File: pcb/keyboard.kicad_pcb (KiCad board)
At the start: 2 copper layers, 21 parts, among them SW1 SW_Push, SW10 RotaryEncoder_Switch, SW2 SW_Push, SW3 SW_Push, SW4 SW_Push, SW5 SW_Push, SW6 SW_Push, SW7 SW_Push, SW8 SW_Push, SW9 SW_Push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

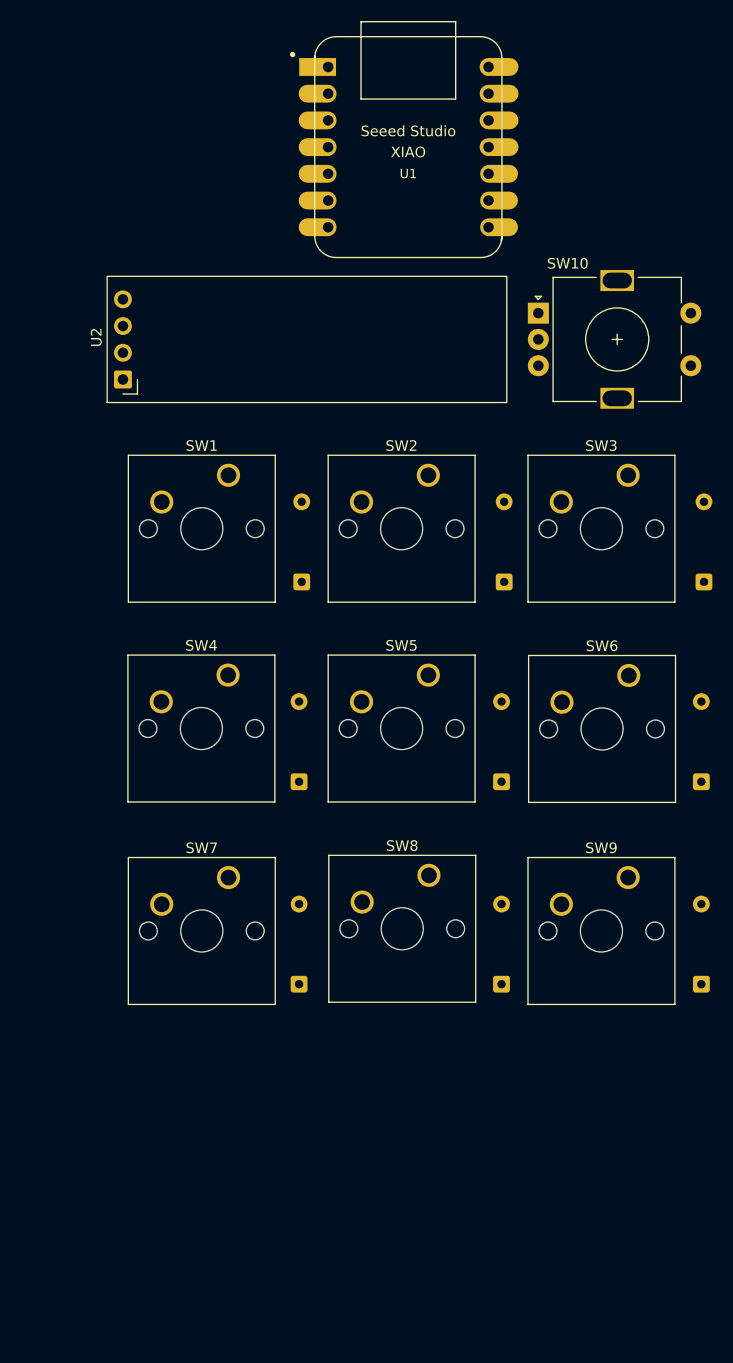
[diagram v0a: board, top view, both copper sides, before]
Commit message: connect switches to the microcontroller
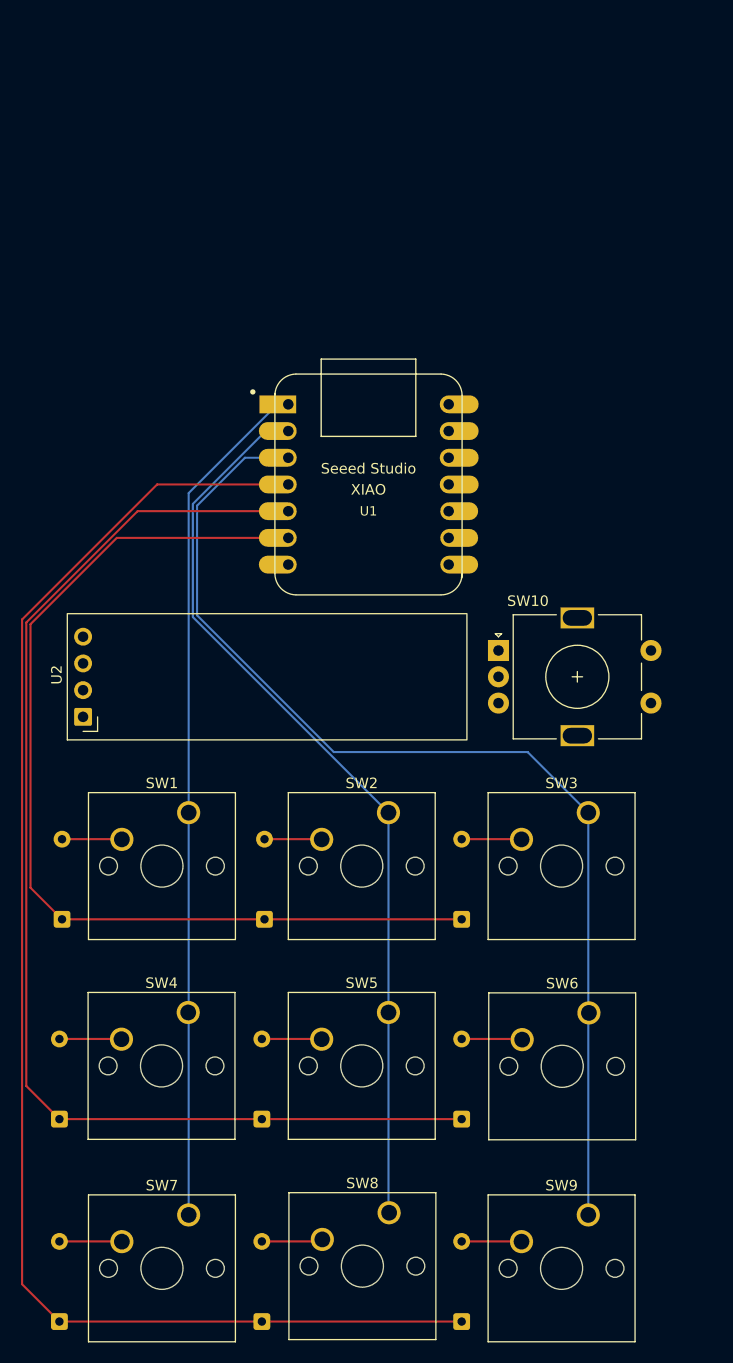
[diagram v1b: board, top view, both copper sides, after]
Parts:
- moved D3 39.5 mm to (131.2, 96.1)
- moved D1 39.4 mm to (93.2, 96.1)
- moved D2 39.4 mm to (112.5, 96.1)
- moved D4 39.4 mm to (93.0, 115.1)
- moved D5 39.4 mm to (112.2, 115.1)
- moved D6 39.4 mm to (131.2, 115.1)
- moved D7 39.4 mm to (93.0, 134.4)
- moved D8 39.4 mm to (112.2, 134.4)
- moved D9 39.4 mm to (131.2, 134.4)
- moved SW6 32.3 mm to (143.3, 105.0)
- moved SW8 32.3 mm to (124.3, 124.0)
- moved SW1 32.3 mm to (105.2, 86.0)
- moved SW10 32.3 mm to (134.7, 70.6)
- moved SW2 32.3 mm to (124.2, 86.0)
- moved SW3 32.3 mm to (143.2, 86.0)
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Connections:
- U1 pad 4: Row 0 -> Row 2
- U1 pad 6: Row 2 -> Row 0
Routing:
- net Row 2: track 0.00 -> 137.1 mm
- net Row 1: track 0.00 -> 116.1 mm
- net Column 2: track 0.00 -> 104.2 mm
- net Row 0: track 0.00 -> 95.2 mm
- net Column 1: track 0.00 -> 87.1 mm
- net Column 0: track 0.00 -> 81.6 mm
- net Net-(D7-A): track 0.00 -> 5.95 mm
- net Net-(D4-A): track 0.00 -> 5.91 mm
- net Net-(D8-A): track 0.00 -> 5.83 mm
- net Net-(D6-A): track 0.00 -> 5.77 mm
- net Net-(D5-A): track 0.00 -> 5.70 mm
- net Net-(D1-A): track 0.00 -> 5.70 mm
- net Net-(D9-A): track 0.00 -> 5.70 mm
- net Net-(D3-A): track 0.00 -> 5.70 mm
- net Net-(D2-A): track 0.00 -> 5.45 mm

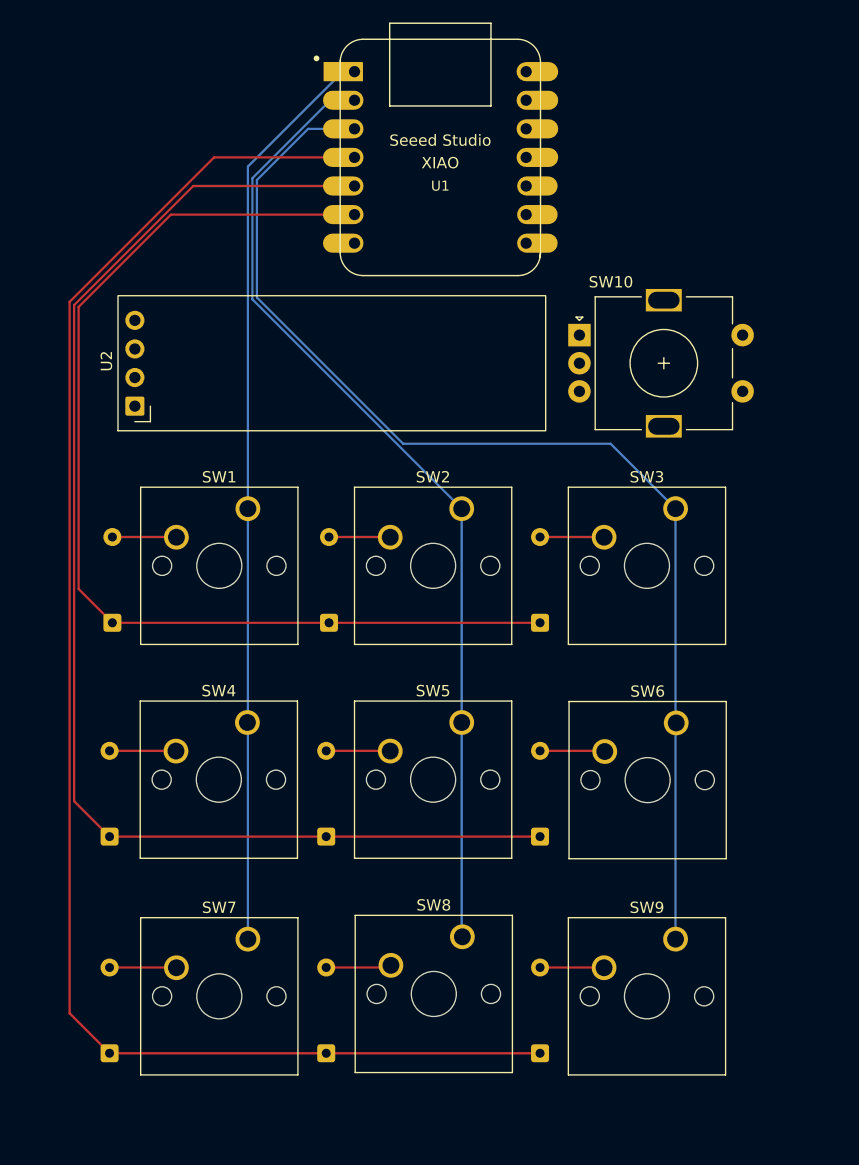
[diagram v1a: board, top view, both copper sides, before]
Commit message: connect all components on schematic; remove invalid connections on pcb
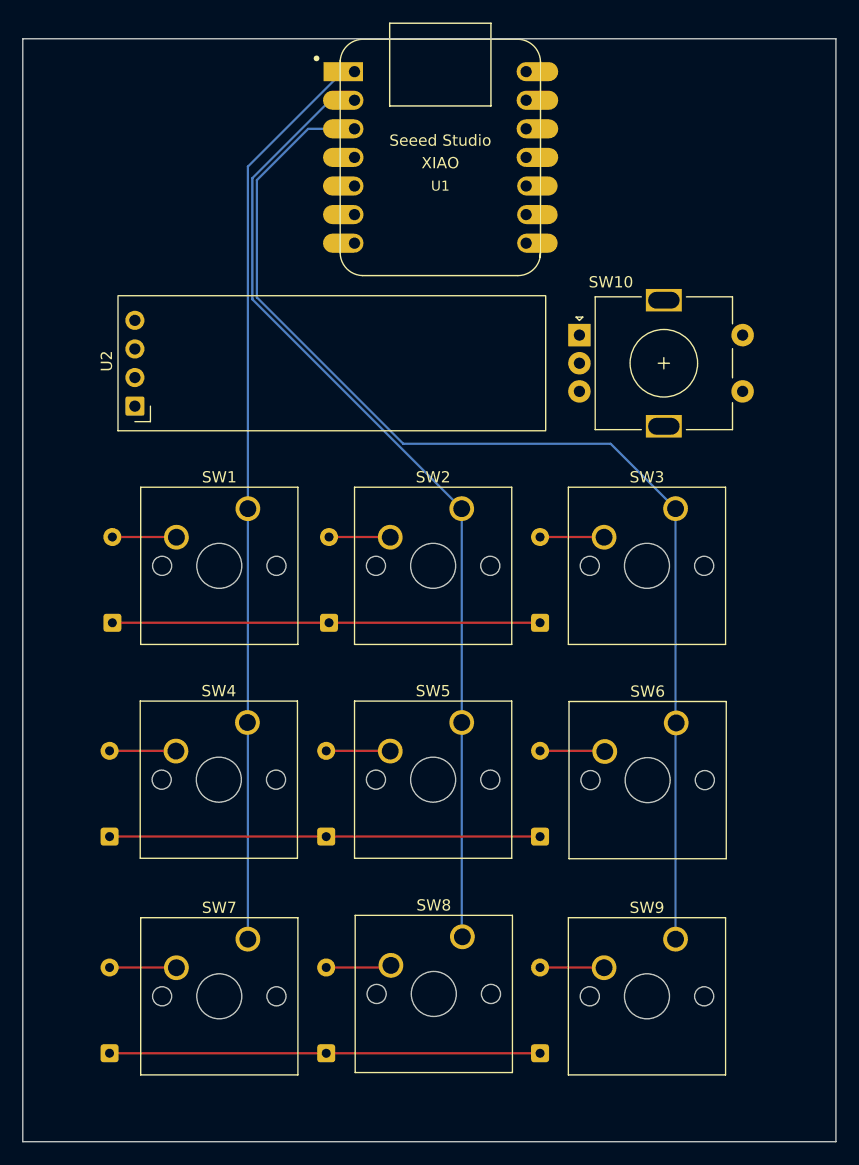
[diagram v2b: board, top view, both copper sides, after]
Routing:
- net Row 2: track 137.1 -> 38.3 mm
- net Row 1: track 116.1 -> 38.3 mm
- net Row 0: track 95.2 -> 38.0 mm
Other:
- board outline added: 72.2 x 98 mm
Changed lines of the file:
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@@
 		)
+	)
+	(gr_rect
+		(start 85.25 44.25)
+		(end 157.5 142.25)
+		(stroke
+			(width 0.05)
+			(type default)
+		)
+		(fill no)
+		(layer "Edge.Cuts")
 	)
 	(segment
@@
 	)
 	(segment
-		(start 90.21 68.08)
-		(end 90.21 93.14)
-		(width 0.2)
-		(layer "F.Cu")
-		(net "Row 0")
-	)
-	(segment
 		(start 93.21 96.14)
 		(end 131.21 96.14)
-		(width 0.2)
-		(layer "F.Cu")
-		(net "Row 0")
-	)
-	(segment
-		(start 98.417985 59.872015)
-		(end 90.21 68.08)
-		(width 0.2)
-		(layer "F.Cu")
-		(net "Row 0")
-	)
-	(segment
-		(start 114.7245 59.872015)
-		(end 98.417985 59.872015)
-		(width 0.2)
-		(layer "F.Cu")
-		(net "Row 0")
-	)
-	(segment
-		(start 90.21 93.14)
-		(end 93.21 96.14)
 		(width 0.2)
 		(layer "F.Cu")
@@
 		(start 92.96 115.14)
 		(end 131.21 115.14)
-		(width 0.2)
-		(layer "F.Cu")
-		(net "Row 1")
-	)
-	(segment
-		(start 114.7245 57.332015)
-		(end 100.3923 57.332015)
-		(width 0.2)
-		(layer "F.Cu")
-		(net "Row 1")
-	)
-	(segment
-		(start 100.3923 57.332015)
-		(end 89.81 67.914315)
-		(width 0.2)
-		(layer "F.Cu")
-		(net "Row 1")
-	)
-	(segment
-		(start 89.81 67.914315)
-		(end 89.81 111.99)
-		(width 0.2)
-		(layer "F.Cu")
-		(net "Row 1")
-	)
-	(segment
-		(start 89.81 111.99)
-		(end 92.96 115.14)
 		(width 0.2)
 		(layer "F.Cu")
@@
 	)
 	(segment
-		(start 89.41 67.63)
-		(end 89.41 130.84)
-		(width 0.2)
-		(layer "F.Cu")
-		(net "Row 2")
-	)
-	(segment
-		(start 102.247985 54.792015)
-		(end 89.41 67.63)
-		(width 0.2)
-		(layer "F.Cu")
-		(net "Row 2")
-	)
-	(segment
-		(start 89.41 130.84)
-		(end 92.96 134.39)
-		(width 0.2)
-		(layer "F.Cu")
-		(net "Row 2")
-	)
-	(segment
-		(start 114.7245 54.792015)
-		(end 102.247985 54.792015)
-		(width 0.2)
-		(layer "F.Cu")
-		(net "Row 2")
-	)
-	(segment

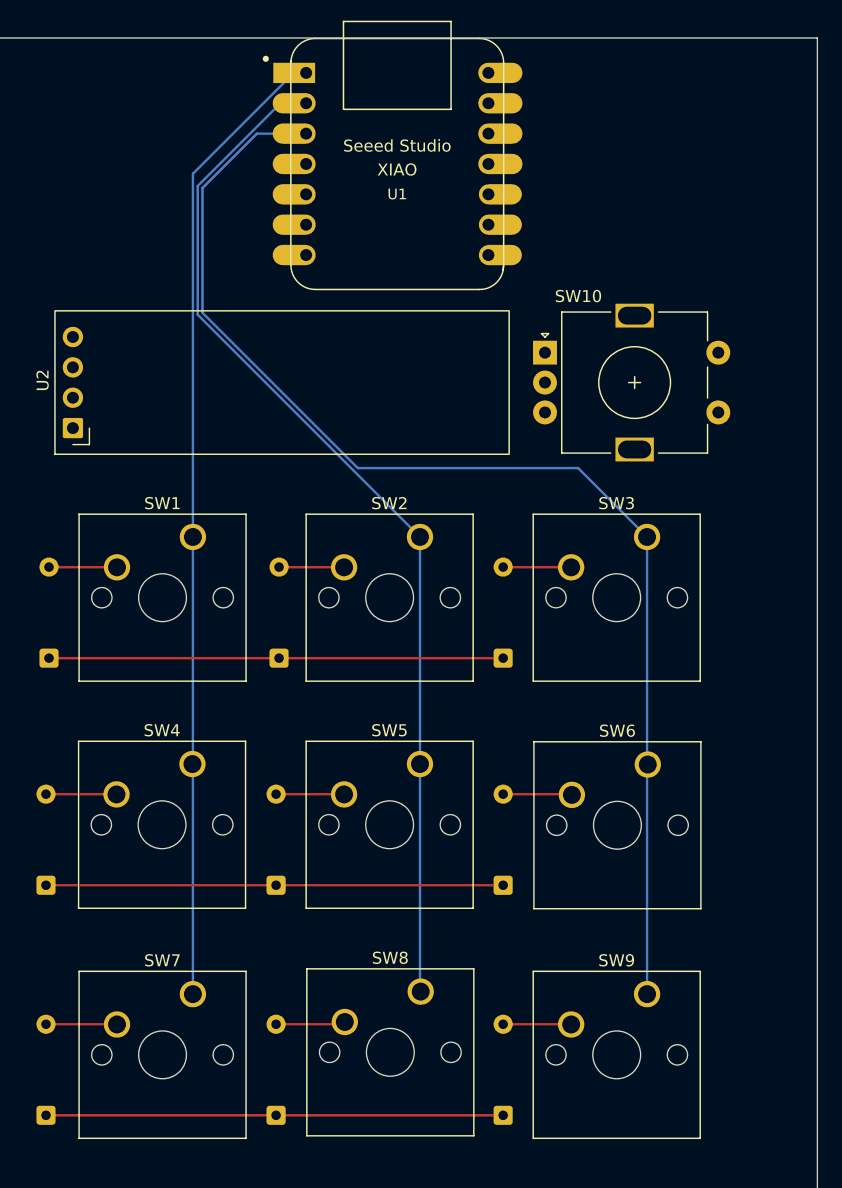
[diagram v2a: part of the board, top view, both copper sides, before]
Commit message: connect everything on the pcb
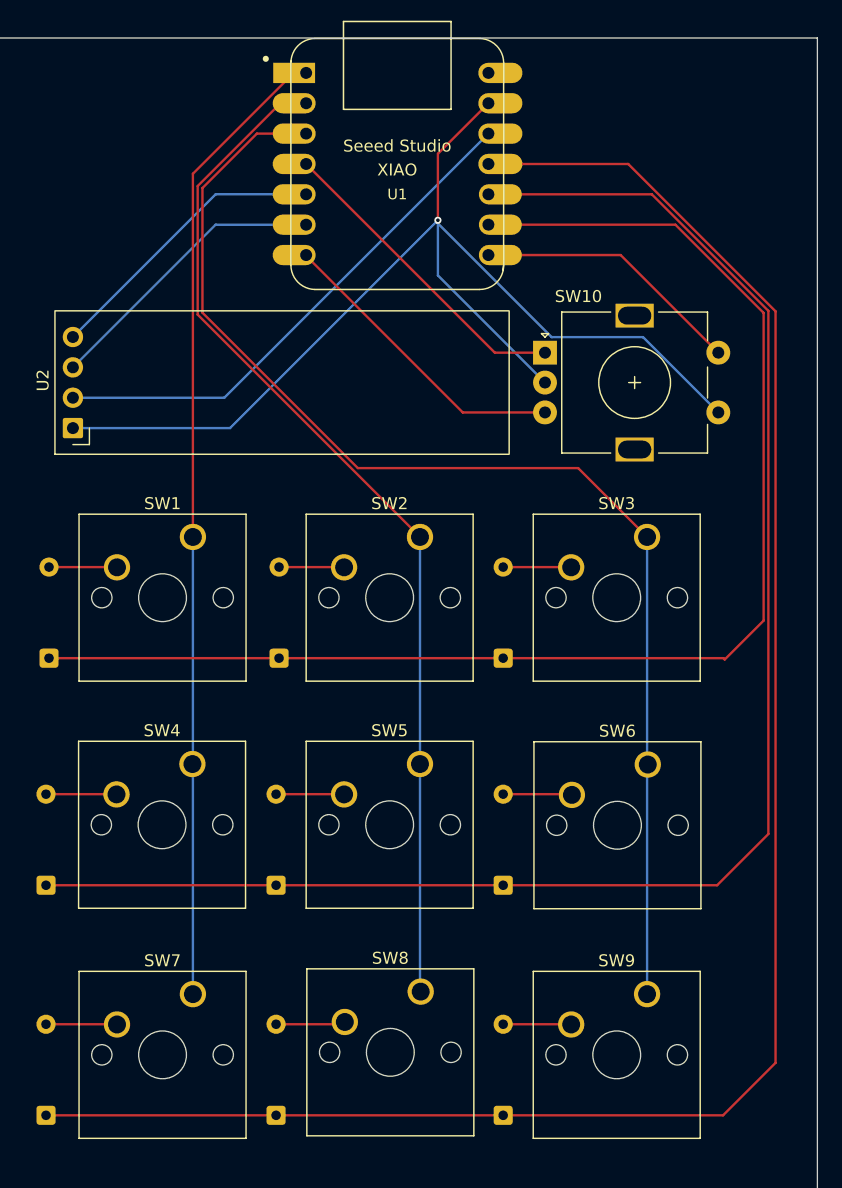
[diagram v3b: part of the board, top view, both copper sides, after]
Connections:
- SW10 pad A: unconnected-(SW10-PadA) -> ROT A
- SW10 pad B: unconnected-(SW10-PadB) -> ROT B
- SW10 pad C: unconnected-(SW10-PadC) -> GND
- SW10 pad S1: unconnected-(SW10-PadS1) -> GND
- SW10 pad S2: unconnected-(SW10-PadS2) -> ROT SWITCH
- U1 pad 10: unconnected-(U1-PA5_A9_D9_MISO-Pad10) -> Row 1
- U1 pad 11: unconnected-(U1-PA6_A10_D10_MOSI-Pad11) -> Row 2
- U1 pad 12: unconnected-(U1-3V3-Pad12) -> VCC
- U1 pad 13: unconnected-(U1-GND-Pad13) -> GND
- U1 pad 4: Row 2 -> ROT A
- U1 pad 5: Row 1 -> SDA
- U1 pad 6: Row 0 -> SCL
- U1 pad 7: unconnected-(U1-PB08_A6_D6_TX-Pad7) -> ROT B
- U1 pad 8: unconnected-(U1-PB09_A7_D7_RX-Pad8) -> ROT SWITCH
- U1 pad 9: unconnected-(U1-PA7_A8_D8_SCK-Pad9) -> Row 0
- U2 pad 1: unconnected-(U2-GND-Pad1) -> GND
- U2 pad 2: unconnected-(U2-VCC-Pad2) -> VCC
- U2 pad 3: unconnected-(U2-SCL-Pad3) -> SCL
- U2 pad 4: unconnected-(U2-SDA-Pad4) -> SDA
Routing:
- net Row 2: track 38.3 -> 154.9 mm
- net GND: track 0.00 -> 96.8 mm, vias 0 -> 1
- net Row 1: track 38.3 -> 133.4 mm
- net Row 0: track 38.0 -> 113.0 mm
- net VCC: track 0.00 -> 43.9 mm
- net ROT A: track 0.00 -> 26.5 mm
- net ROT B: track 0.00 -> 25.5 mm
- net SCL: track 0.00 -> 24.5 mm
- net SDA: track 0.00 -> 24.5 mm
- net ROT SWITCH: track 0.00 -> 22.6 mm

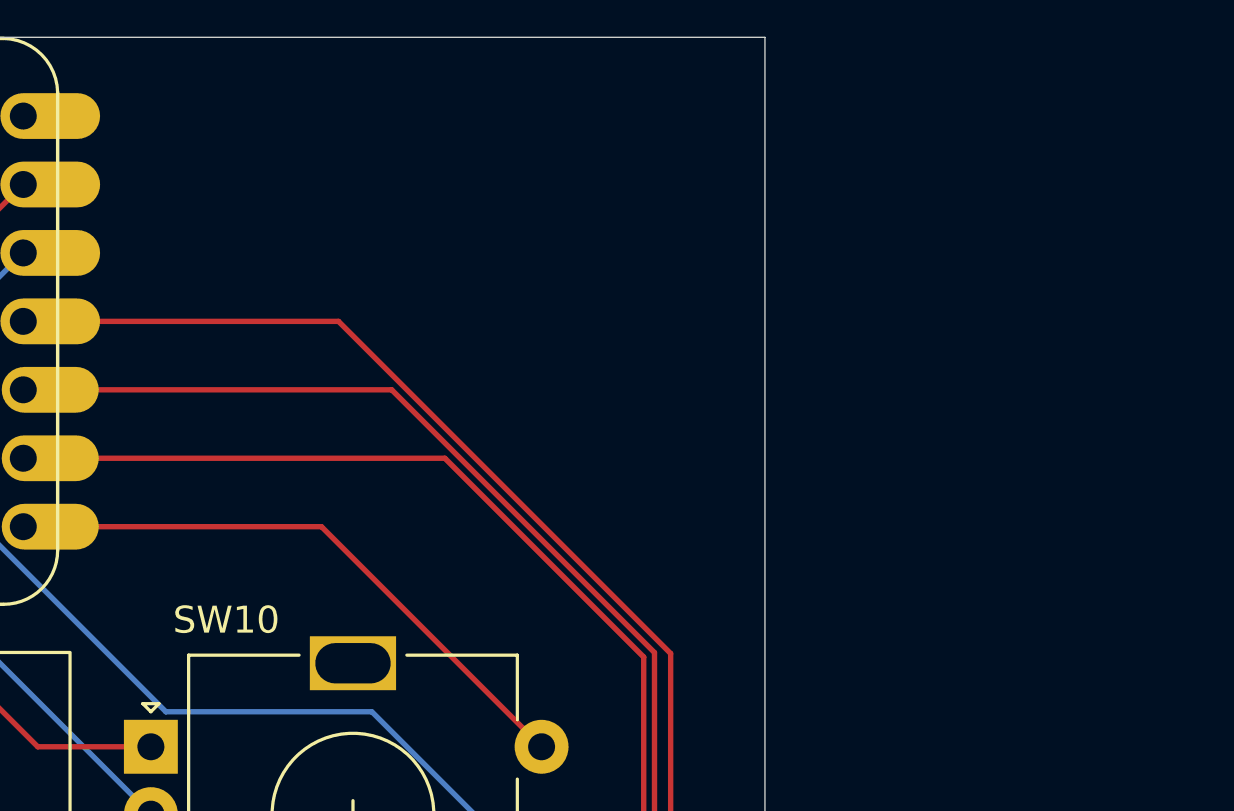
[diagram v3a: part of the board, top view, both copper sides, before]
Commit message: add rgb leds to schematic; update power labels; remove a switch and add rotary knob one to matrix instead
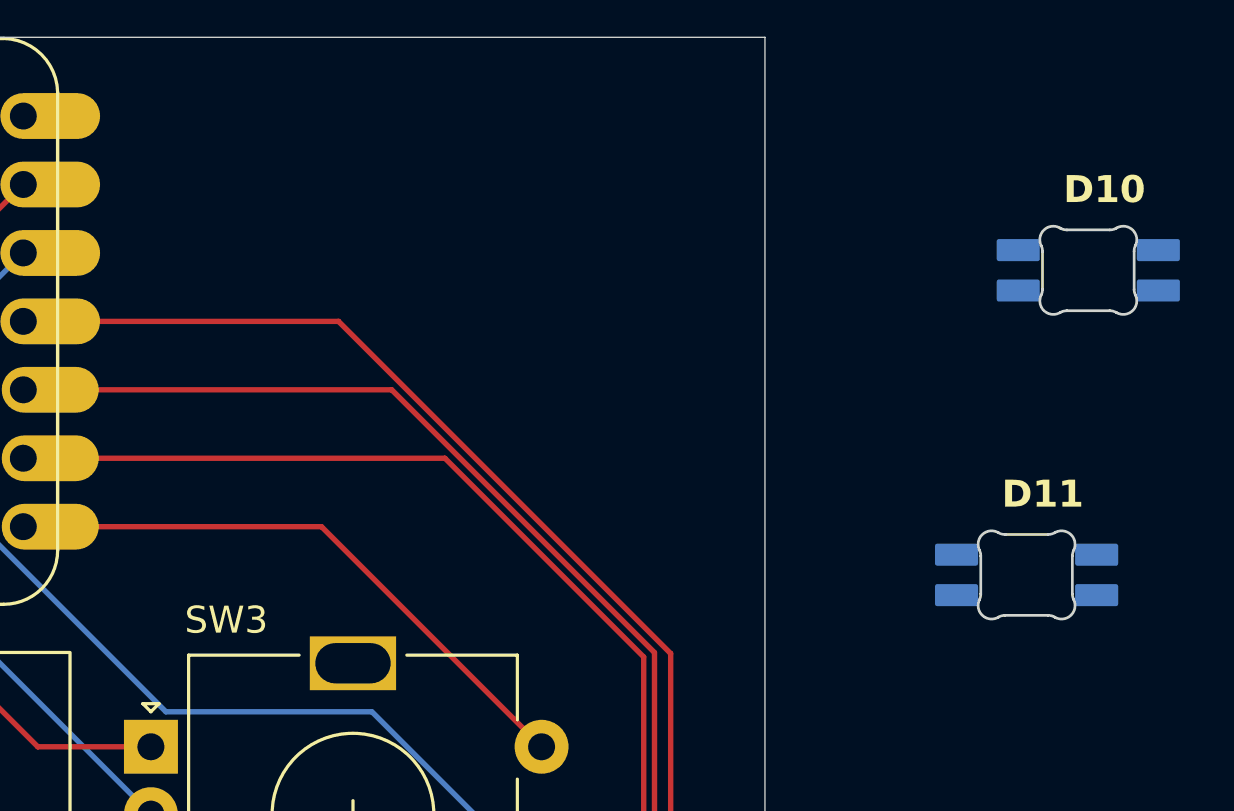
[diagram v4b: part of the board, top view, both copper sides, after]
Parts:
- added D10: SK6812MINI-E, footprints:SK6812MINI-E_fixed, F.Cu at (169.5, 53.0)
- added D11: SK6812MINI-E, footprints:SK6812MINI-E_fixed, F.Cu at (167.2, 64.3)
- renumbered SW10 to SW3
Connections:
- D3 pad 2: Net-(D3-A) -> ROT S2
- SW3 pad S1: GND -> Column 2
- SW3 pad S2: ROT SWITCH -> ROT S2
- U1 pad 12: VCC -> unconnected-(U1-3V3-Pad12)
- U1 pad 14: unconnected-(U1-5V-Pad14) -> VCC
- U1 pad 8: ROT SWITCH -> unconnected-(U1-PB09_A7_D7_RX-Pad8)
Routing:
- net ROT SWITCH: track 22.6 -> 0.00 mm
- net (no net): track 0.00 -> 22.6 mm
